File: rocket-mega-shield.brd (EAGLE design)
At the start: 118 x 55 mm, 70 parts, among them J1 1X2-3.5MM, J2 1X2-3.5MM

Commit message: working on revision 2, not done yet
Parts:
- removed 55GACCEL: AD22286-R2, kurt:LCC8
- removed 5VREG: NCP1117DT50G, kurt:DPAK
- removed ANALOGV: AYZ0202, SparkFun-Electromechanical:AYZ0202
- removed C5: 10uF, adafruit:C1206
- removed C6: 0.1uF, adafruit:C1206
- removed PWRMUX: TPS2111APWR, kurt:TSSOP8
- removed R9: 3.3k, adafruit:R1206
- added 200GACCEL: ADXL377, zortness:LFCSP-16
- added C19, C20, C26: 0.01uF, adafruit:C1206
- added D1: (no value), SparkFun-DiscreteSemi:SMA-DIODE_ALT
- added FIRST, FOURTH, SECOND, THIRD: MOSFET-NCHANNELSI7112DN, SparkFun-DiscreteSemi:POWERPAK1212-8
- added PYRO: 1X6TERMINALBLOCK, zortness:1X6TERMINALBLOCK
- C1: value 10uF -> 100uF
- C4: value 0.1uF -> 100uF
- R1: value 400 -> 10k
- R6, R8: value 1.7k -> 10k
- R7: value 3.3k -> 10k
- moved R8 131.6 mm to (-3.00, -88.0), turned to 0 degrees
- moved R7 124.7 mm to (-3.00, -82.0), turned to 0 degrees
- moved R6 118.0 mm to (-3.00, -76.0), turned to 0 degrees
- moved R1 105.9 mm to (-3.00, -70.0), turned to 0 degrees
- moved C7 87.9 mm to (-3.00, -17.0)
- moved C1 83.1 mm to (-3.00, -57.0), flipped to the top, turned to 0 degrees
- moved C4 71.7 mm to (-3.00, -51.0), flipped to the top
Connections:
- removed net 5VOUT: 5VREG.4, C5.2, C6.1, PWRMUX.2, PWRMUX.8
- removed net BATT_RAW: 5VREG.3, C1.1, C24.1, C25.1, EXTBATT.2, RELAY1.6, RELAY2.6
- removed net VCC5: 3.3VREG.3, 55GACCEL.1, 55GACCEL.7, 55GACCEL.8, C2.1, C7.1, PWRMUX.7
- new net N$1: D1.A, EXTBATT.2
- new net N$24: FOURTH.D1, FOURTH.D2, FOURTH.D3, FOURTH.D4, FOURTH.DPAD, PYRO.6
- new net VIN: 3.3VREG.3, C2.1, C24.1, C25.1, D1.C, MEGA.VIN, PYRO.1, PYRO.2, RELAY1.6, RELAY2.6
- net GND: now also 200GACCEL.6, 200GACCEL.7, C19.2, C20.2, C26.2, FIRST.S1, FIRST.S2, FIRST.S3, FOURTH.S1, FOURTH.S2, FOURTH.S3, SECOND.S1, SECOND.S2, SECOND.S3, THIRD.S1, THIRD.S2, THIRD.S3; no longer 55GACCEL.3, 5VREG.1, C5.1, C6.2, PWRMUX.1, PWRMUX.3, PWRMUX.5, R1.1, R6.2, R7.2, R8.1, R9.1
- net MEGA5V: no longer C4.1, PWRMUX.6
- net MEGAA0: now also 200GACCEL.5, C19.1; no longer ANALOGV.3, R6.1, R7.1
- net MEGAA1: now also 200GACCEL.4, C20.1; no longer ANALOGV.6, R8.2, R9.2
- net MEGAA2: now also 200GACCEL.16, C26.1; no longer ANALOGV.1
- net MEGAA3: no longer ANALOGV.4
- net N$3: now also FIRST.D1, FIRST.D2, FIRST.D3, FIRST.D4, FIRST.DPAD, PYRO.3; no longer 55GACCEL.2, ANALOGV.5
- net N$4: now also PYRO.4, SECOND.D1, SECOND.D2, SECOND.D3, SECOND.D4, SECOND.DPAD; no longer PWRMUX.4, R1.2
- net N$9: now also PYRO.5, THIRD.D1, THIRD.D2, THIRD.D3, THIRD.D4, THIRD.DPAD; no longer 55GACCEL.6, ANALOGV.2
- net VCC3: now also 200GACCEL.14, 200GACCEL.15, C1.1, C4.1, C7.1
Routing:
- net BATT_RAW: track 81.2 -> 0.00 mm
- net VIN: track 0.00 -> 80.4 mm
- net VCC5: track 53.1 -> 0.00 mm, vias 2 -> 0
- net N$3: track 42.2 -> 0.00 mm
- net 5VOUT: track 28.2 -> 0.00 mm, vias 1 -> 0
- net N$9: track 24.1 -> 0.00 mm
- net MEGAA1: track 36.4 -> 23.8 mm
- net N$4: track 4.50 -> 0.00 mm
- net MEGAA0: track 21.4 -> 18.2 mm

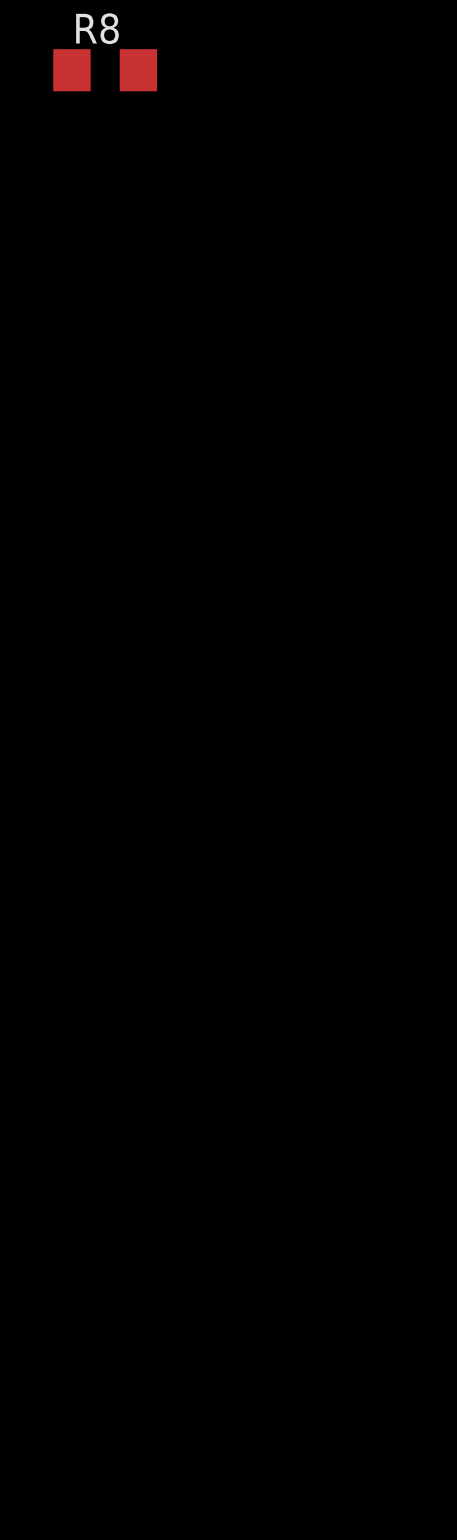
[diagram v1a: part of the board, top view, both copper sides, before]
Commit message: initial schematic with mosfets and continuity checking
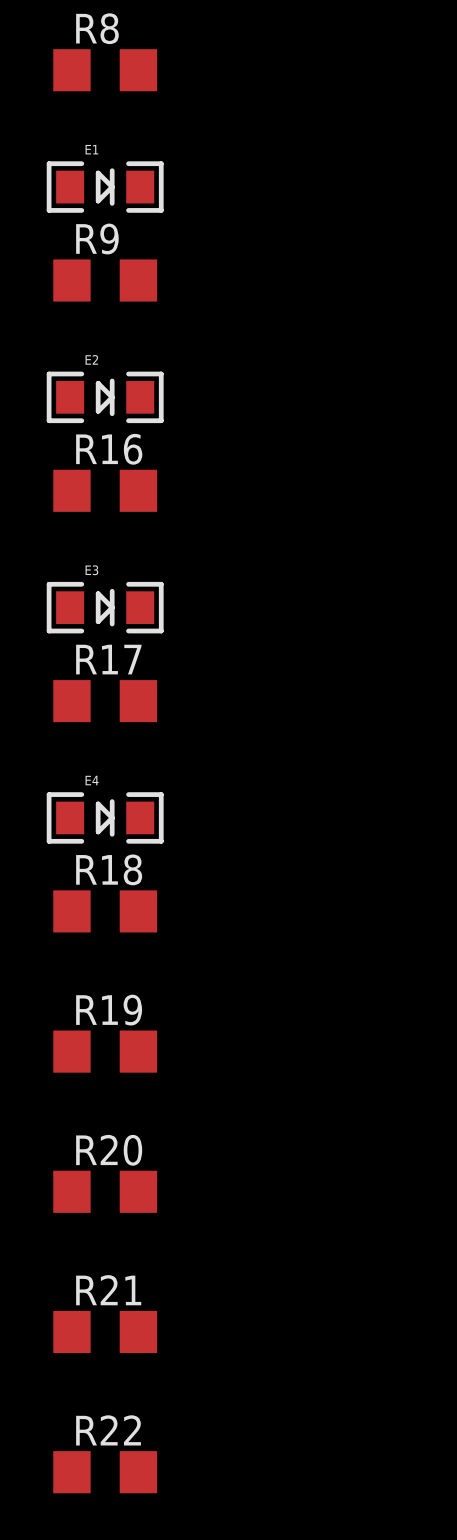
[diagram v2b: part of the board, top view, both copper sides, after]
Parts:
- added E1, E2, E3, E4: (no value), SparkFun-LED:LED-1206
- added R16, R17, R18, R9: 330, adafruit:R1206
- added R19, R20, R21, R22: 500k, adafruit:R1206
- FIRST, FOURTH, SECOND, THIRD: value MOSFET-NCHANNELSI7112DN -> SI7112DN
- R1, R6, R7, R8: value 10k -> 10M
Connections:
- removed net N$1: D1.A, EXTBATT.2
- new net BATT+: D1.A, EXTBATT.2, PYRO.1, PYRO.2
- new net MOSFET1: E4.A, FIRST.G, R1.2
- new net MOSFET2: E3.A, R6.2, SECOND.G
- new net MOSFET3: E2.A, R7.2, THIRD.G
- new net MOSFET4: E1.A, FOURTH.G, R8.2
- new net N$29: E1.C, R9.1
- new net N$30: E2.C, R16.1
- new net N$31: E3.C, R17.1
- new net N$32: E4.C, R18.1
- new net N$33: R19.1
- new net N$34: R20.1
- new net N$35: R21.1
- new net N$36: R22.1
- net GND: now also R1.1, R16.2, R17.2, R18.2, R6.1, R7.1, R8.1, R9.2
- net N$24: now also R19.2
- net N$3: now also R22.2
- net N$4: now also R21.2
- net N$9: now also R20.2
- net VIN: no longer PYRO.1, PYRO.2

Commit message: working on layout for rev2
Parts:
- removed C24, C25: 100uF, SparkFun-Capacitors:CPOL-RADIAL-100UF-25V
- removed GPSSELECT: AYZ0202, SparkFun-Electromechanical:AYZ0202
- removed J1, J2: 1X2-3.5MM, adafruit:1X2-3.5MM
- removed R11, R12: 330, adafruit:R1206
- removed RE1, RE2: (no value), SparkFun-LED:LED-1206
- removed RELAY1, RELAY2: PVN012PbF, kurt:PVN012PBF_SMT6
- removed SDCONV, SERCONV: M74HC4050M, SparkFun-DigitalIC:SO016
- added CONT: CD4050, zortness:SOIC16
- added CONV: M74HC4050M, SparkFun-DigitalIC:SO016
- C4: value 100uF -> 220uF; device adafruit:C1206 -> adafruit:C1210
- moved R22 175.1 mm to (40.6, 21.6), flipped to the bottom
- moved R21 173.0 mm to (40.6, 25.4), flipped to the bottom
- moved R20 170.9 mm to (40.6, 29.2), flipped to the bottom
- moved R19 168.8 mm to (40.6, 33.0), flipped to the bottom
- moved E4 147.9 mm to (24.1, 25.4)
- moved R18 142.0 mm to (30.5, 14.0), flipped to the bottom, turned to 180 degrees
- moved R17 136.9 mm to (30.5, 17.8), flipped to the bottom, turned to 180 degrees
- moved E3 136.6 mm to (24.1, 22.9)
- moved R16 131.9 mm to (30.5, 21.6), flipped to the bottom, turned to 180 degrees
- moved R9 126.9 mm to (30.5, 25.4), flipped to the bottom, turned to 180 degrees
- moved E2 125.3 mm to (24.1, 20.3)
- moved R8 116.6 mm to (24.1, 25.4), flipped to the bottom
- moved E1 114.1 mm to (24.1, 17.8)
- moved R7 107.1 mm to (24.1, 21.6), flipped to the bottom
- moved R6 97.6 mm to (24.1, 17.8), flipped to the bottom
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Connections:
- removed net MEGAA3: MEGA.A3
- removed net MEGARE1: MEGA.42, R12.1
- removed net MEGARE2: MEGA.43, R11.1
- removed net MOSFET1: E4.A, FIRST.G, R1.2
- removed net MOSFET2: E3.A, R6.2, SECOND.G
- removed net MOSFET3: E2.A, R7.2, THIRD.G
- removed net MOSFET4: E1.A, FOURTH.G, R8.2
- removed net N$11: GPS.P$9, GPSSELECT.5
- removed net N$12: GPS.P$10, GPSSELECT.2
- removed net N$19: RE2.C, RELAY2.1
- removed net N$2: RE1.C, RELAY1.1
- removed net N$20: R11.2, RE2.A
- removed net N$23: R12.2, RE1.A
- removed net R1OUT: J1.2, RELAY1.5
- removed net R2OUT: J2.2, RELAY2.5
- removed net TX2: GPSSELECT.3, SERCONV.2
- new net CONT1: CONT.2, MEGA.38
- new net CONT2: CONT.4, MEGA.39
- new net CONT3: CONT.6, MEGA.40
- new net CONT4: CONT.10, MEGA.41
- new net PYRO1: E1.A, FIRST.G, MEGA.42, R1.2
- new net PYRO2: E2.A, MEGA.43, R6.2, SECOND.G
- new net PYRO3: E3.A, MEGA.44, R7.2, THIRD.G
- new net PYRO4: E4.A, FOURTH.G, MEGA.45, R8.2
- net GND: now also CONT.8, CONV.8; no longer C24.2, C25.2, J1.1, J2.1, RELAY1.2, RELAY2.2, SDCONV.8, SERCONV.8
- net MEGAMOSI: now also CONV.7; no longer SDCONV.3
- net MEGARX1: now also GPS.P$9; no longer GPSSELECT.4, XBEESELECT.6
- net MEGARX2: no longer GPSSELECT.6
- net MEGASCLK: now also CONV.9; no longer SDCONV.5
- net MEGASDCS: now also CONV.11; no longer SDCONV.7
- net MEGATX0: now also CONV.3; no longer SERCONV.7
- net MEGATX1: now also CONV.5; no longer SERCONV.5
- net MEGATX2: no longer SERCONV.3
- net MOSI: now also CONV.6; no longer SDCONV.2
- net N$29: now also E4.C; no longer E1.C
- net N$30: now also E3.C; no longer E2.C
- net N$31: now also E2.C; no longer E3.C
- net N$32: now also E1.C; no longer E4.C
- net N$33: now also CONT.9
- net N$34: now also CONT.7
- net N$35: now also CONT.5
- net N$36: now also CONT.3
- net SCLK: now also CONV.10; no longer SDCONV.4
- net SDCS: now also CONV.12; no longer SDCONV.6
- net TX0: now also CONV.2; no longer SERCONV.6
- net TX1: now also CONV.4, GPS.P$10; no longer GPSSELECT.1, SERCONV.4, XBEESELECT.3
- net VCC3: now also CONT.1, CONV.1; no longer SDCONV.1, SERCONV.1
- net VIN: no longer C24.1, C25.1, RELAY1.6, RELAY2.6
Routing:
- net GND: track 0.29 -> 552.1 mm, vias 38 -> 1
- net MEGARE2: track 119.3 -> 0.00 mm
- net PYRO1: track 0.00 -> 105.8 mm, vias 0 -> 1
- net MEGARE1: track 103.7 -> 0.00 mm
- net PYRO4: track 0.00 -> 92.3 mm, vias 0 -> 1
- net PYRO2: track 0.00 -> 92.3 mm, vias 0 -> 2
- net PYRO3: track 0.00 -> 87.7 mm, vias 0 -> 2
- net MEGAMOSI: track 75.8 -> 0.00 mm
- net MEGASCLK: track 75.7 -> 0.00 mm
- net N$4: track 0.00 -> 69.8 mm
- net MEGASDCS: track 61.6 -> 0.00 mm
- net TX1: track 58.2 -> 0.00 mm, vias 1 -> 0
- net TX0: track 56.3 -> 0.00 mm, vias 1 -> 0
- net N$3: track 0.00 -> 52.5 mm, vias 0 -> 1
- net VIN: track 80.4 -> 32.3 mm, vias 0 -> 1
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- removed copper zone on layer 1, net GND
- removed copper zone on layer 16, net GND
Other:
- board size 118 x 55 mm -> 160 x 100 mm
- board text removed: "RocketDuino V1"

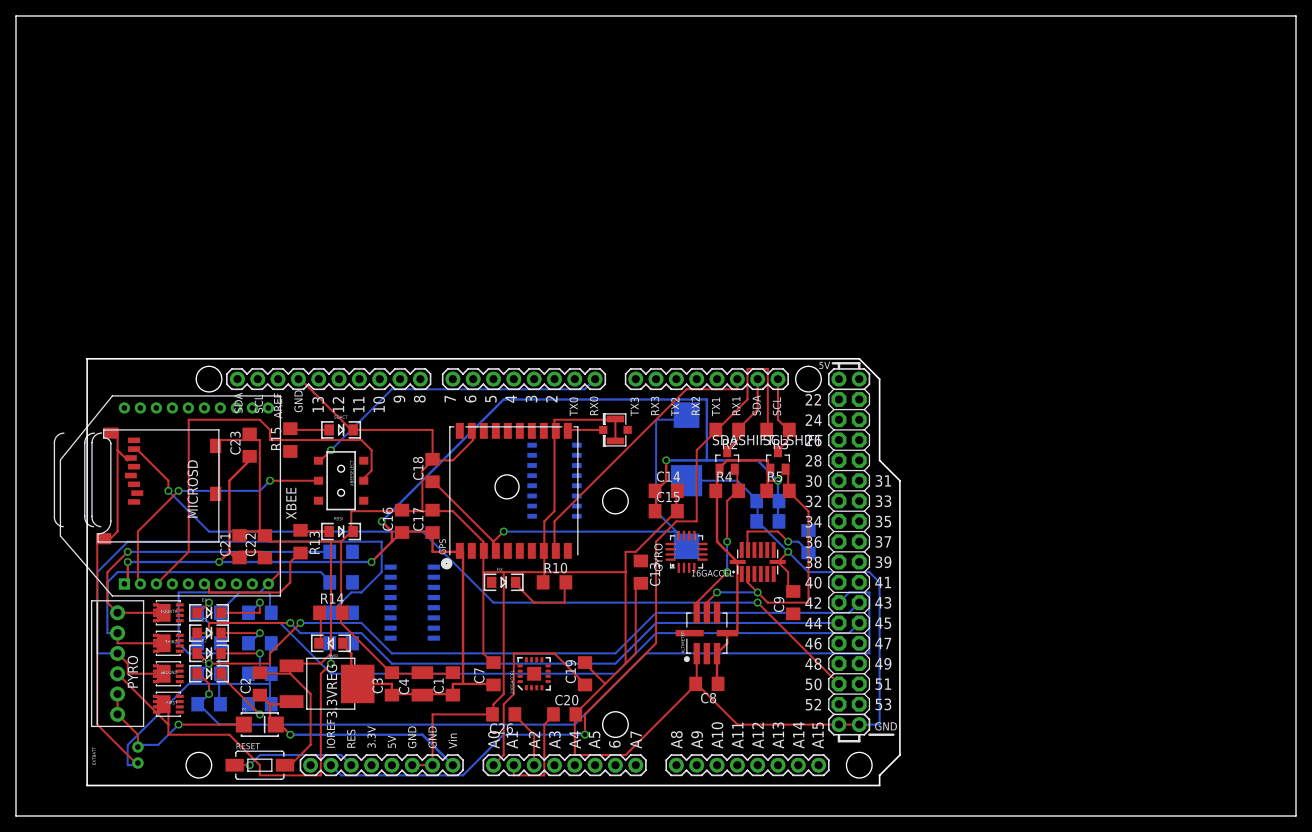
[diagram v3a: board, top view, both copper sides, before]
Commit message: mostly done with schematic and layout... still need to add fuse and clean up labeling
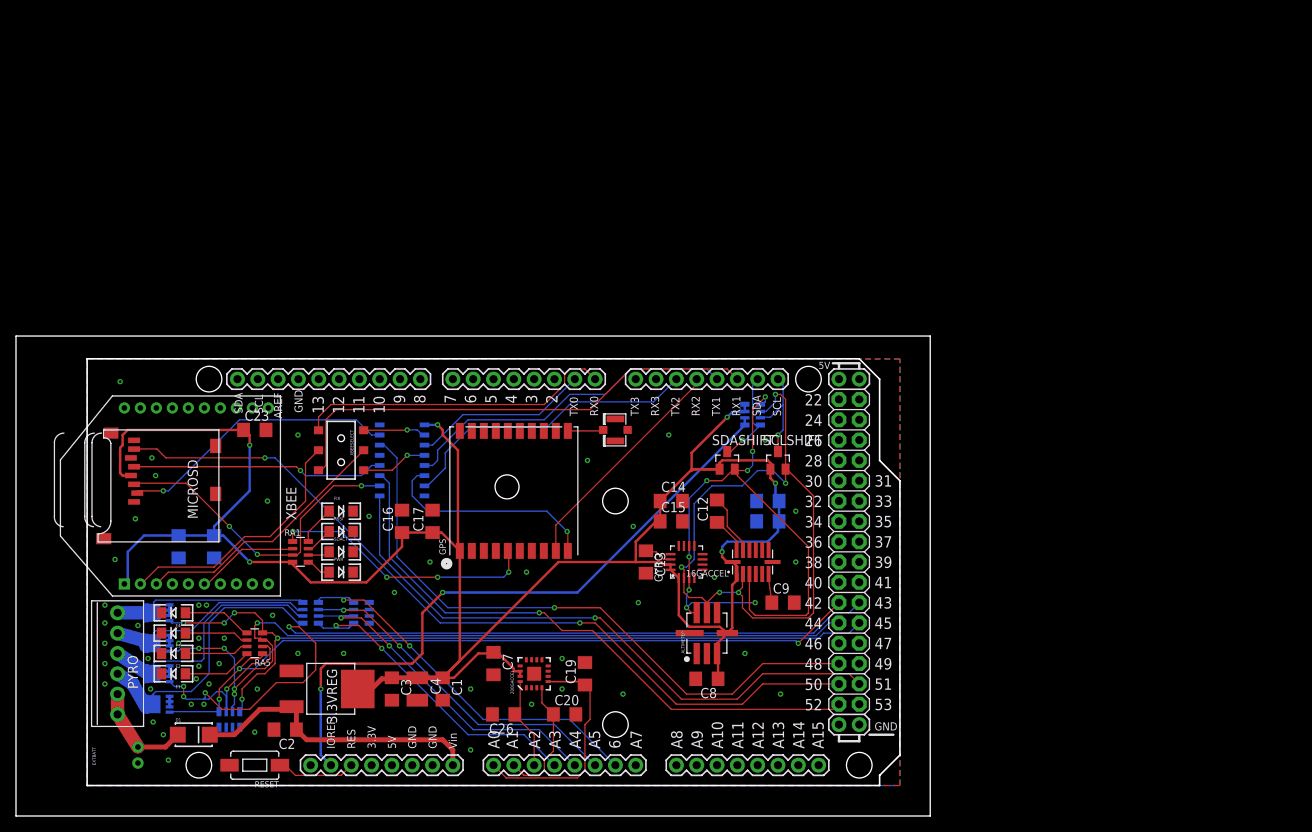
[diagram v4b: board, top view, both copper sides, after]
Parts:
- removed C18: 1uF, adafruit:C1206
- removed CONT: CD4050, zortness:SOIC16
- removed GPSBATT: (no value), adafruit:CR1220-SMD
- removed R1, R6, R7, R8: 10M, adafruit:R1206
- removed R10, R16, R17, R18, R9: 330, adafruit:R1206
- removed R13, R14, R15: 1k, adafruit:R1206
- removed R19, R20, R21, R22: 500k, adafruit:R1206
- removed R2, R3, R4, R5: 10k, adafruit:R1206
- added RA1, RA5: 330, zortness:1206X4RESISTORARRAY
- added RA2, RA6: 10k, zortness:1206X4RESISTORARRAY
- added RA3: 620k, zortness:1206X4RESISTORARRAY
- added RA4: 110k, zortness:1206X4RESISTORARRAY
- C2: value 10uF -> 100uF16V
- D1: value (none) -> STTH102A
- moved FIX 22.2 mm to (40.6, 38.1)
- moved CONV 19.2 mm to (48.3, 44.5), turned to 270 degrees
- moved SDACT 15.2 mm to (40.6, 33.0)
- moved C12 12.0 mm to (87.6, 38.1), flipped to the top, turned to 90 degrees
- moved PWR 8.98 mm to (40.6, 30.5), turned to 0 degrees
- moved D1 8.35 mm to (22.2, 10.2)
- moved C21 7.62 mm to (20.3, 33.7), flipped to the bottom, turned to 270 degrees
- moved C2 6.54 mm to (33.7, 10.8), turned to 180 degrees
- moved C22 6.35 mm to (24.8, 33.7), flipped to the bottom, turned to 270 degrees
- moved E1 4.45 mm to (19.7, 17.8), turned to 180 degrees
- moved E2 4.45 mm to (19.7, 20.3), turned to 180 degrees
- moved E3 4.45 mm to (19.7, 22.9), turned to 180 degrees
- moved E4 4.45 mm to (19.7, 25.4), turned to 180 degrees
- moved XBEESELECT 3.81 mm to (40.6, 45.7)
- moved C23 2.01 mm to (29.8, 48.3), turned to 0 degrees
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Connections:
- removed net CONT1: CONT.2, MEGA.38
- removed net CONT2: CONT.4, MEGA.39
- removed net CONT3: CONT.6, MEGA.40
- removed net CONT4: CONT.10, MEGA.41
- removed net N$13: C18.1, GPS.P$4, GPSBATT.+$1, GPSBATT.+$2
- removed net N$14: FIX.A, GPS.P$5
- removed net N$15: FIX.C, R10.2
- removed net N$26: R15.2, SDACT.A
- removed net N$29: E4.C, R9.1
- removed net N$30: E3.C, R16.1
- removed net N$31: E2.C, R17.1
- removed net N$32: E1.C, R18.1
- removed net N$33: CONT.9, R19.1
- removed net N$34: CONT.7, R20.1
- removed net N$35: CONT.5, R21.1
- removed net N$36: CONT.3, R22.1
- removed net N$9: PYRO.5, R20.2, THIRD.D1, THIRD.D2, THIRD.D3, THIRD.D4, THIRD.DPAD
- new net GPSFIX: GPS.P$5, RA1.1
- new net MEGAA3: MEGA.A3, RA3.4, RA4.5
- new net MEGAA4: MEGA.A4, RA3.3, RA4.6
- new net MEGAA5: MEGA.A5, RA3.2, RA4.7
- new net MEGAA6: MEGA.A6, RA3.1, RA4.8
- new net N$1: PWR.A, RA1.5
- new net N$11: RA1.7, RSSI.A
- new net N$12: FIX.A, RA1.8
- new net N$19: E1.A, RA5.8
- new net N$2: RA1.6, SDACT.A
- new net N$25: PYRO.5, RA3.7, THIRD.D1, THIRD.D2, THIRD.D3, THIRD.D4, THIRD.DPAD
- new net TX2: CONV.6, GPS.P$10
- new net XRSSI: RA1.2, XBEE.6
- net GND: now also E1.C, E2.C, E3.C, E4.C, FIX.C, PWR.C, RA4.1, RA4.2, RA4.3, RA4.4, RA6.5, RA6.6, RA6.7, RA6.8; no longer C18.2, CONT.8, GPSBATT.-, R1.1, R10.1, R14.2, R16.2, R17.2, R18.2, R6.1, R7.1, R8.1, R9.2
- net IOREF: now also RA2.1, RA2.2; no longer R2.2, R3.2
- net MEGAMOSI: now also CONV.9; no longer CONV.7
- net MEGARX1: now also XBEESELECT.6; no longer GPS.P$9
- net MEGARX2: now also GPS.P$9
- net MEGASCL: now also RA2.7; no longer R3.1
- net MEGASCLK: now also CONV.11; no longer CONV.9
- net MEGASDA: now also RA2.8; no longer R2.1
- net MEGASDCS: now also CONV.14; no longer CONV.11
- net MEGATX2: now also CONV.7
- net MOSI: now also CONV.10, RA1.3; no longer CONV.6, R15.1
- net N$16: now also E4.A, RA5.5; no longer PWR.C, R14.1
- net N$17: now also E3.A, RA5.6; no longer R13.2, XBEE.6
- net N$18: now also E2.A, RA5.7; no longer R13.1, RSSI.A
- net N$24: now also RA3.8; no longer R19.2
- net N$3: now also RA3.5; no longer R22.2
- net N$4: now also RA3.6; no longer R21.2
- net PYRO1: now also RA5.1, RA6.1; no longer E1.A, R1.2
- net PYRO2: now also RA5.2, RA6.2; no longer E2.A, R6.2
- net PYRO3: now also RA5.3, RA6.3; no longer E3.A, R7.2
- net PYRO4: now also RA5.4, RA6.4; no longer E4.A, R8.2
- net SCL: now also RA2.6; no longer R5.2
- net SCLK: now also CONV.12; no longer CONV.10
- net SDA: now also RA2.5; no longer R4.2
- net SDCS: now also CONV.15; no longer CONV.12
- net TX1: now also XBEESELECT.3; no longer GPS.P$10
- net VCC3: now also RA1.4, RA2.3, RA2.4; no longer CONT.1, PWR.A, R4.1, R5.1
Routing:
- net GND: track 552.1 -> 5.28 mm, vias 1 -> 52
- net MEGASDCS: track 0.00 -> 79.1 mm, vias 0 -> 1
- net MEGAMOSI: track 0.00 -> 76.6 mm, vias 0 -> 1
- net MEGASCLK: track 0.00 -> 75.2 mm, vias 0 -> 1
- net SDA: track 20.4 -> 78.9 mm, vias 2 -> 8
- net N$13: track 57.7 -> 0.00 mm, vias 1 -> 0
- net MEGAA6: track 0.00 -> 48.8 mm, vias 0 -> 2
- net SCL: track 36.4 -> 84.3 mm, vias 2 -> 5
- net MEGAA5: track 0.00 -> 45.1 mm, vias 0 -> 2
- net N$9: track 43.8 -> 0.00 mm
- net MEGAA4: track 0.00 -> 42.9 mm, vias 0 -> 2
- net MEGATX1: track 0.00 -> 42.8 mm
- net MEGAA3: track 0.00 -> 41.1 mm, vias 0 -> 2
- net MOSI: track 0.00 -> 40.5 mm, vias 0 -> 3
- net MEGATX2: track 0.00 -> 38.1 mm
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- added copper zone on layer 1, net GND
- added copper zone on layer 16, net GND
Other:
- board size 160 x 100 mm -> 114.3 x 60 mm
